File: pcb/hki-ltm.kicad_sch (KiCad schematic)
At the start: 15 parts, among them J1 Connector, USB-TYPE-C-16P, U1 ESP32-C3FH4

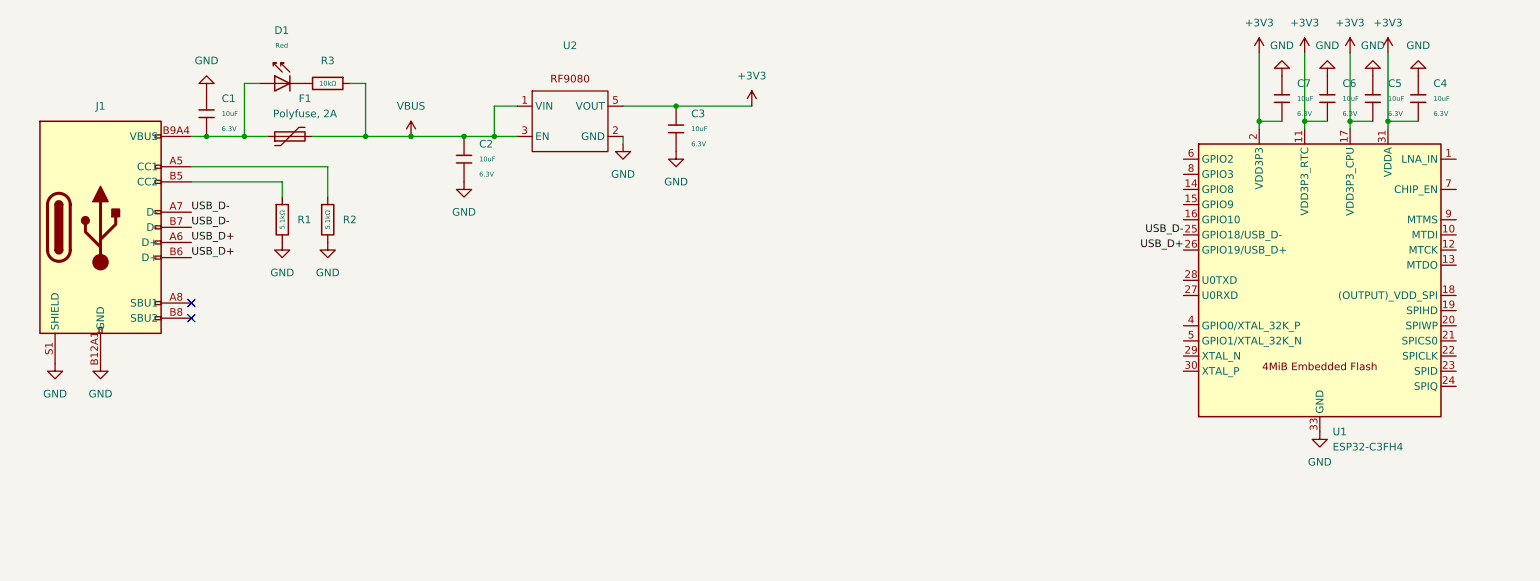
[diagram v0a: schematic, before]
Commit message: More schematic power system work
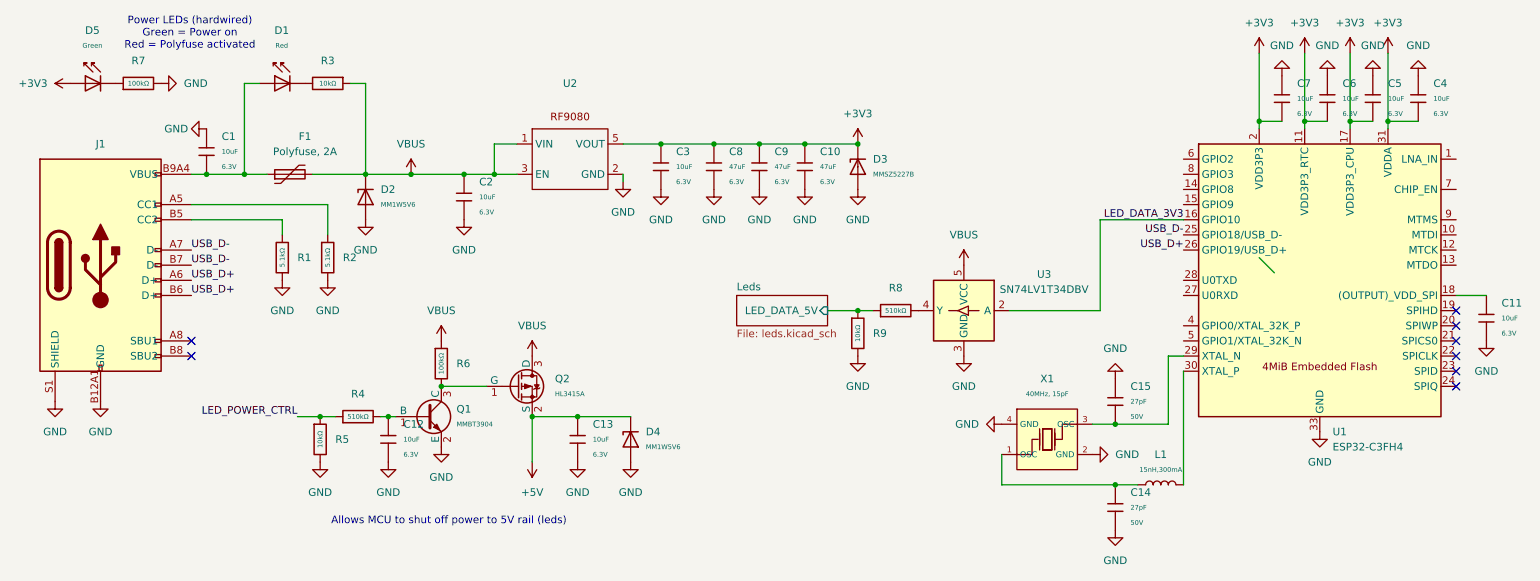
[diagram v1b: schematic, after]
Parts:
- added C10, C8, C9: 47uF, PCM_JLCPCB:C_0805, symbol PCM_JLCPCB-Capacitors:0805,47uF
- added C11, C12, C13: 10uF, PCM_JLCPCB:C_0402, symbol PCM_JLCPCB-Capacitors:0402,10uF
- added C14, C15: 27pF, PCM_JLCPCB:C_0402, symbol PCM_JLCPCB-Capacitors:0402,27pF
- added D2, D4: MM1W5V6, PCM_JLCPCB:D_SOD-123, symbol PCM_JLCPCB-Diodes:Zener,MM1W5V6
- added D3: MMSZ5227B, PCM_JLCPCB:D_SOD-123, symbol PCM_JLCPCB-Diodes:Zener,MMSZ5227B
- added D5: Green, PCM_JLCPCB:D_0805, symbol PCM_JLCPCB-Diodes:LED,0805,Green
- added L1: 15nH,300mA, PCM_JLCPCB:L_0402, symbol PCM_JLCPCB-Inductors:15nH,300mA
- added Q1: MMBT3904, PCM_JLCPCB:Q_SOT-23, symbol PCM_JLCPCB-Transistors:NPN,MMBT3904
- added Q2: HL3415A, PCM_JLCPCB:Q_SOT-23, symbol PCM_JLCPCB-Transistors:PMOS,HL3415A
- added R4, R8: 510kΩ, PCM_JLCPCB:R_0402, symbol PCM_JLCPCB-Resistors:0402,510kΩ
- added R5, R9: 10kΩ, PCM_JLCPCB:R_0402, symbol PCM_JLCPCB-Resistors:0402,10kΩ
- added R6, R7: 100kΩ, PCM_JLCPCB:R_0402, symbol PCM_JLCPCB-Resistors:0402,100kΩ
- added U3: SN74LV1T34DBV, Package_TO_SOT_SMD:SOT-23-5, symbol Logic_LevelTranslator:SN74LV1T34DBV
- added X1: 40MHz, 15pF, PCM_JLCPCB:OSC-SMD_4P-L3.2-W2.5-BL_SIT8008BI, symbol PCM_JLCPCB-Extended:Crystal, 40MHz, 15pF
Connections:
- net +3V3: now also C10.1, C8.1, C9.1, D3.1, D5.2
- net GND: now also R1.1, C10.2, C11.2, C12.2, C13.2, C14.2, C15.1, C8.2, C9.2, D2.2, D3.2, D4.2, Q1.2 (E), R5.2, R7.2, R9.2, U3.3 (GND), X1.2 (GND), X1.4 (GND); no longer R1.2
- net VBUS: now also D2.1, Q2.3 (D), R6.1, U3.5 (VCC)
- net at J1.B5 (CC2): now also R1.2; no longer R1.1
- net LED_DATA_3V3: now reaches U1.16 (GPIO10)
- net LED_DATA_3V3: now also U3.2 (A)
- net at U1.18 ((OUTPUT)_VDD_SPI): now also C11.1
- net at U1.29 (XTAL_N): now also C15.2, X1.3 (OSC)
- net at U1.30 (XTAL_P): now also L1.2
- new net: Q1.3 (C), Q2.1 (G), R6.2
- new net: R8.2, U3.4 (Y)
- new net: C12.1, Q1.1 (B), R4.2
- new net: C14.1, L1.1, X1.1 (OSC)
- new net: D5.1, R7.1
- new net +5V: C13.1, D4.1, Q2.2 (S)
- new net LED_POWER_CTRL: R4.1, R5.1
- new net Leds/LED_DATA_5V: R8.1, R9.1
- no-connect marks 2 -> 8
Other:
- added sheet Leds (leds.kicad_sch)
- note added: "Allows MCU to shut off power to 5V rail (leds)"
- note added: "Power LEDs (hardwired) Green = Power on Red = Polyfuse activated"
- title: (none) -> Finland Live Train Map
- moved on the sheet: C1, C2, C3, F1, J1, R1, R2, U2
